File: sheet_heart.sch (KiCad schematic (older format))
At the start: 41 parts, among them P1 CONN_02X05, P7 CONN_01X01, P8 CONN_01X01, U4 STM32F042GxU

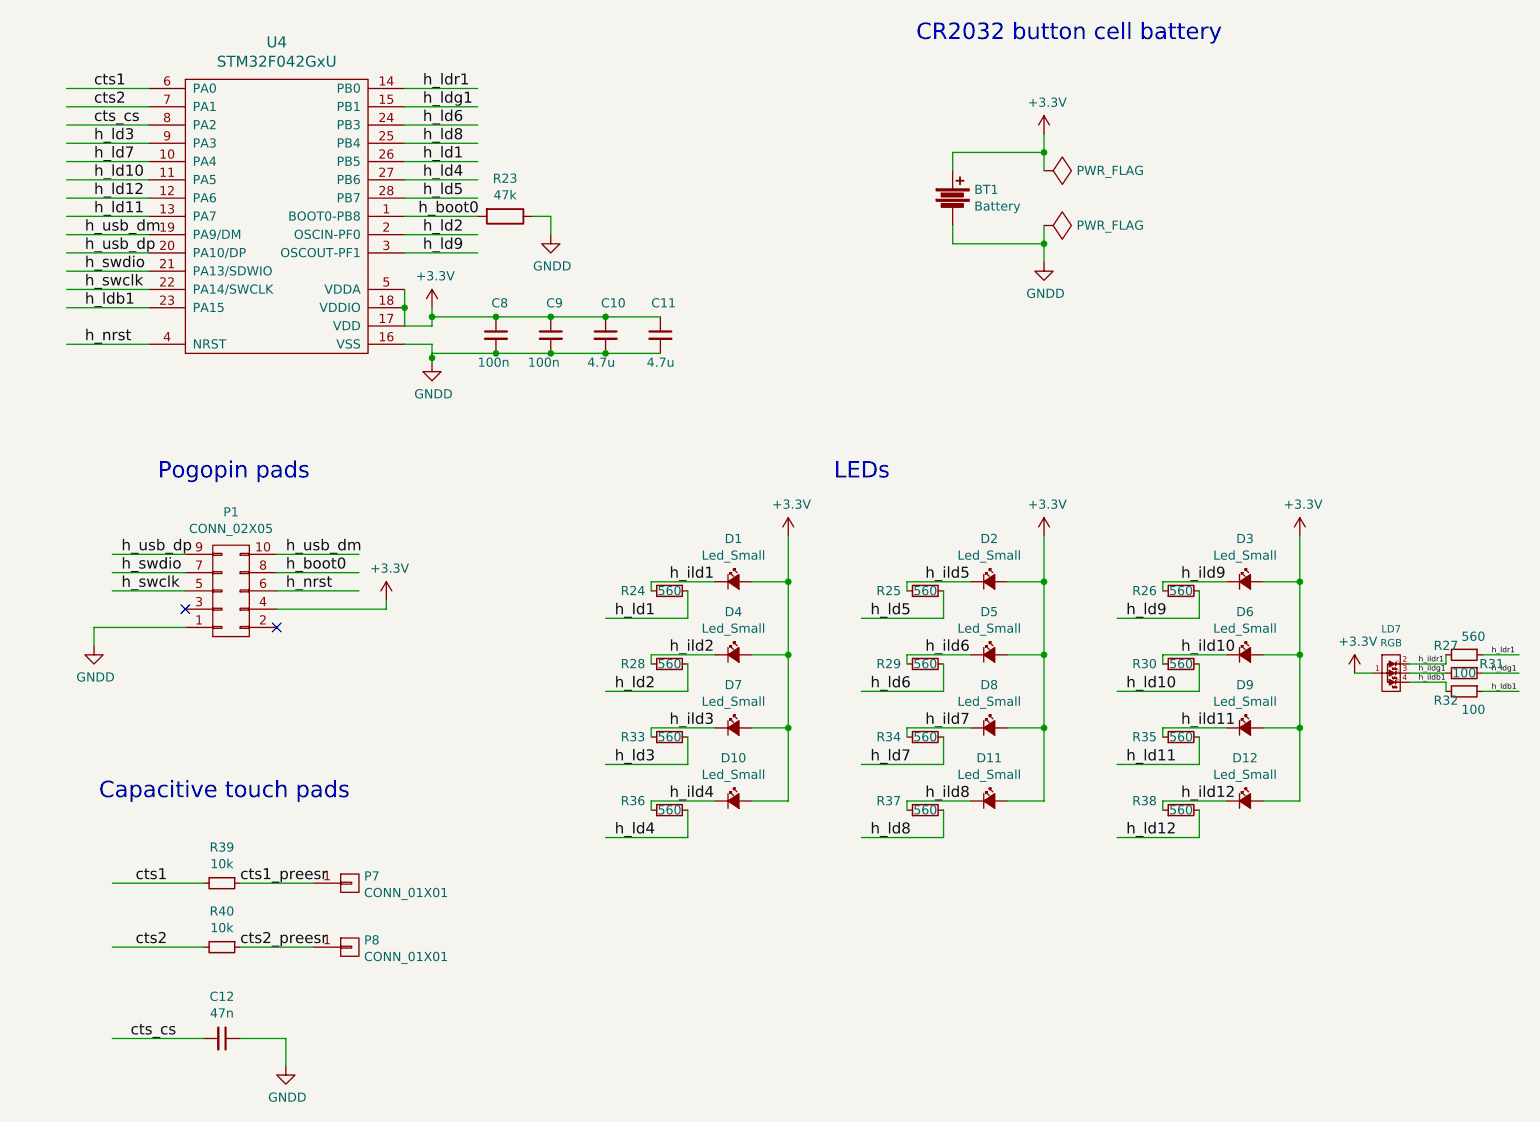
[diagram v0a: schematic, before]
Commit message: Routing cleanup and silkscreen on heart.
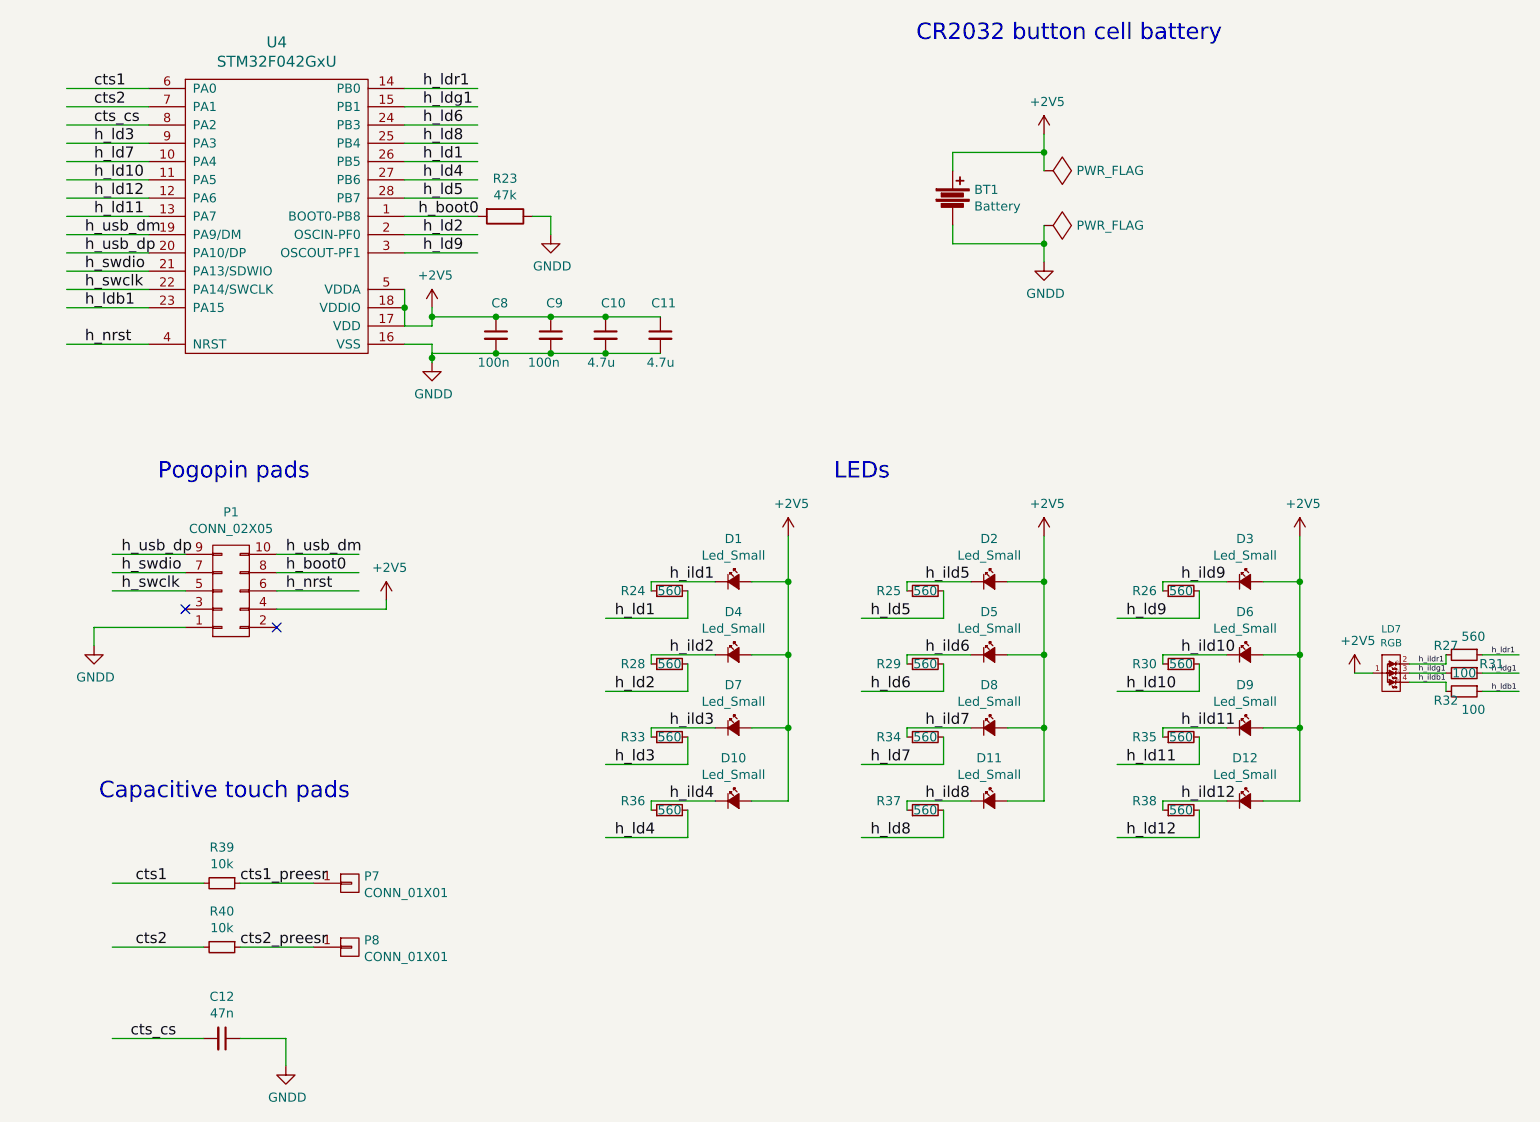
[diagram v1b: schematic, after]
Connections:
- net labels added: +2V5
- net labels removed: +3.3V
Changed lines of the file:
@@
-$EndComp
-$Comp
-L +3.3V #PWR025
-U 1 1 5774F8B9
-P 3400 4400
-F 0 "#PWR025" H 3400 4250 50  0001 C CNN
-F 1 "+3.3V" H 3418 4573 50  0000 C CNN
-F 2 "" H 3400 4400 50  0000 C CNN
-F 3 "" H 3400 4400 50  0000 C CNN
-	1    3400 4400
-	1    0    0    -1
-$EndComp
-$Comp
-L +3.3V #PWR026
-U 1 1 5774FA26
-P 3650 2800
-F 0 "#PWR026" H 3650 2650 50  0001 C CNN
-F 1 "+3.3V" H 3668 2973 50  0000 C CNN
-F 2 "" H 3650 2800 50  0000 C CNN
-F 3 "" H 3650 2800 50  0000 C CNN
-	1    3650 2800
-	1    0    0    -1
-$EndComp
-$Comp
-L +3.3V #PWR027
-U 1 1 5774FC19
-P 8700 4800
-F 0 "#PWR027" H 8700 4650 50  0001 C CNN
-F 1 "+3.3V" H 8718 4973 50  0000 C CNN
-F 2 "" H 8700 4800 50  0000 C CNN
-F 3 "" H 8700 4800 50  0000 C CNN
-	1    8700 4800
-	1    0    0    -1
 $EndComp
 $Comp
@@
 $EndComp
 $Comp
-L GNDD #PWR028
+L GNDD #PWR025
 U 1 1 57764FC5
 P 7000 2550
-F 0 "#PWR028" H 7000 2300 50  0001 C CNN
+F 0 "#PWR025" H 7000 2300 50  0001 C CNN
 F 1 "GNDD" H 7008 2377 50  0000 C CNN
 F 2 "" H 7000 2550 50  0000 C CNN
@@
 $EndComp
 $Comp
-L +3.3V #PWR029
-U 1 1 577651B8
-P 7000 1850
-F 0 "#PWR029" H 7000 1700 50  0001 C CNN
-F 1 "+3.3V" H 7018 2023 50  0000 C CNN
-F 2 "" H 7000 1850 50  0000 C CNN
-F 3 "" H 7000 1850 50  0000 C CNN
-	1    7000 1850
-	1    0    0    -1
-$EndComp
-$Comp
-L PWR_FLAG #FLG030
+L PWR_FLAG #FLG026
 U 1 1 577652E9
 P 7000 2050
-F 0 "#FLG030" H 7000 2145 50  0001 C CNN
+F 0 "#FLG026" H 7000 2145 50  0001 C CNN
 F 1 "PWR_FLAG" V 7000 2228 50  0000 L CNN
 F 2 "" H 7000 2050 50  0000 C CNN
@@
 $EndComp
 $Comp
-L PWR_FLAG #FLG031
+L PWR_FLAG #FLG027
 U 1 1 577656BA
 P 7000 2350
-F 0 "#FLG031" H 7000 2445 50  0001 C CNN
+F 0 "#FLG027" H 7000 2445 50  0001 C CNN
 F 1 "PWR_FLAG" V 7000 2528 50  0000 L CNN
 F 2 "" H 7000 2350 50  0000 C CNN
@@
 	1    0    0    -1
 $EndComp
-$Comp
-L +3.3V #PWR032
-U 1 1 57768776
-P 5600 4050
-F 0 "#PWR032" H 5600 3900 50  0001 C CNN
-F 1 "+3.3V" H 5618 4223 50  0000 C CNN
-F 2 "" H 5600 4050 50  0000 C CNN
-F 3 "" H 5600 4050 50  0000 C CNN
-	1    5600 4050
-	1    0    0    -1
-$EndComp
 Text Label 4950 4300 0    60   ~ 0
 h_ild1
@@
 	1    0    0    -1
 $EndComp
-$Comp
-L +3.3V #PWR033
-U 1 1 5776B1ED
-P 7000 4050
-F 0 "#PWR033" H 7000 3900 50  0001 C CNN
-F 1 "+3.3V" H 7018 4223 50  0000 C CNN
-F 2 "" H 7000 4050 50  0000 C CNN
-F 3 "" H 7000 4050 50  0000 C CNN
-	1    7000 4050
-	1    0    0    -1
-$EndComp
 Text Label 6350 4300 0    60   ~ 0
 h_ild5
@@
 F 3 "" V 8100 5500 50  0000 C CNN
 	1    8100 5500
-	1    0    0    -1
-$EndComp
-$Comp
-L +3.3V #PWR034
-U 1 1 5776B5A9
-P 8400 4050
-F 0 "#PWR034" H 8400 3900 50  0001 C CNN
-F 1 "+3.3V" H 8418 4223 50  0000 C CNN
-F 2 "" H 8400 4050 50  0000 C CNN
-F 3 "" H 8400 4050 50  0000 C CNN
-	1    8400 4050
 	1    0    0    -1
 $EndComp
@@
 Wire Wire Line
 	4300 2300 4300 2400
+$Comp
+L +2V5 #PWR028
+U 1 1 577CBF37
+P 7000 1850
+F 0 "#PWR028" H 7000 1700 50  0001 C CNN
+F 1 "+2V5" H 7018 2027 50  0000 C CNN
+F 2 "" H 7000 1850 50  0000 C CNN
+F 3 "" H 7000 1850 50  0000 C CNN
+	1    7000 1850
+	1    0    0    -1
+$EndComp
+$Comp
+L +2V5 #PWR029
+U 1 1 577CC1D9
+P 3400 4400
+F 0 "#PWR029" H 3400 4250 50  0001 C CNN
+F 1 "+2V5" H 3418 4577 50  0000 C CNN
+F 2 "" H 3400 4400 50  0000 C CNN
+F 3 "" H 3400 4400 50  0000 C CNN
+	1    3400 4400
+	1    0    0    -1
+$EndComp
+$Comp
+L +2V5 #PWR030
+U 1 1 577CC308
+P 5600 4050
+F 0 "#PWR030" H 5600 3900 50  0001 C CNN
+F 1 "+2V5" H 5618 4227 50  0000 C CNN
+F 2 "" H 5600 4050 50  0000 C CNN
+F 3 "" H 5600 4050 50  0000 C CNN
+	1    5600 4050
+	1    0    0    -1
+$EndComp
+$Comp
+L +2V5 #PWR031
+U 1 1 577CC36A
+P 7000 4050
+F 0 "#PWR031" H 7000 3900 50  0001 C CNN
+F 1 "+2V5" H 7018 4227 50  0000 C CNN
+F 2 "" H 7000 4050 50  0000 C CNN
+F 3 "" H 7000 4050 50  0000 C CNN
+	1    7000 4050
+	1    0    0    -1
+$EndComp
+$Comp
+L +2V5 #PWR032
+U 1 1 577CC447
+P 8400 4050
+F 0 "#PWR032" H 8400 3900 50  0001 C CNN
+F 1 "+2V5" H 8418 4227 50  0000 C CNN
+F 2 "" H 8400 4050 50  0000 C CNN
+F 3 "" H 8400 4050 50  0000 C CNN
+	1    8400 4050
+	1    0    0    -1
+$EndComp
+$Comp
+L +2V5 #PWR033
+U 1 1 577CC4A9
+P 8700 4800
+F 0 "#PWR033" H 8700 4650 50  0001 C CNN
+F 1 "+2V5" H 8718 4977 50  0000 C CNN
+F 2 "" H 8700 4800 50  0000 C CNN
+F 3 "" H 8700 4800 50  0000 C CNN
+	1    8700 4800
+	1    0    0    -1
+$EndComp
+$Comp
+L +2V5 #PWR034
+U 1 1 577CC6CE
+P 3650 2800
+F 0 "#PWR034" H 3650 2650 50  0001 C CNN
+F 1 "+2V5" H 3668 2977 50  0000 C CNN
+F 2 "" H 3650 2800 50  0000 C CNN
+F 3 "" H 3650 2800 50  0000 C CNN
+	1    3650 2800
+	1    0    0    -1
+$EndComp
 $EndSCHEMATC
